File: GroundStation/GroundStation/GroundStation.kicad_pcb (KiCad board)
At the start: 2 copper layers, 42 parts, among them J1 SD_Card_Receptacle, J4 Conn_Coaxial, P1 USB_C_Plug_USB2.0, U1 STM32F103C8Tx, U3 LD1117S33TR_SOT223, U9 NEO-M9N-00B

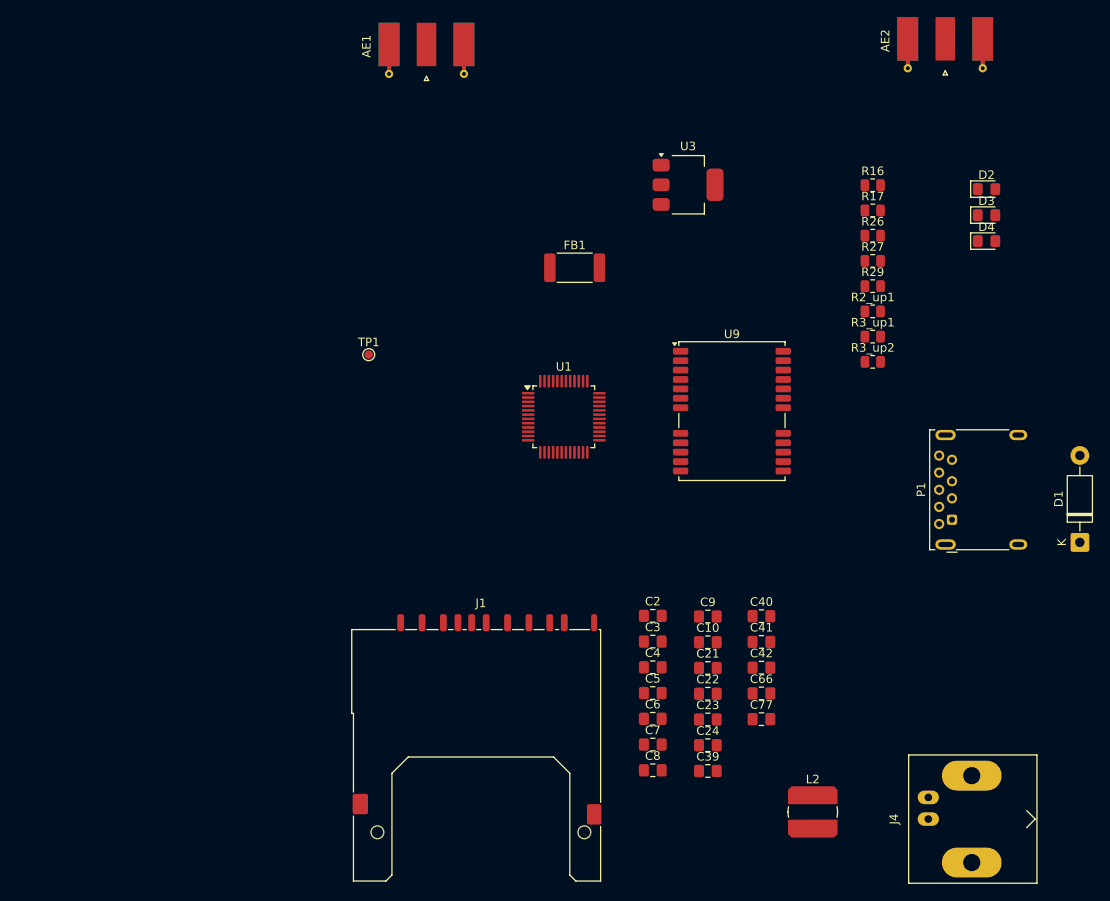
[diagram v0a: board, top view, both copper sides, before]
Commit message: assign package for groundstation
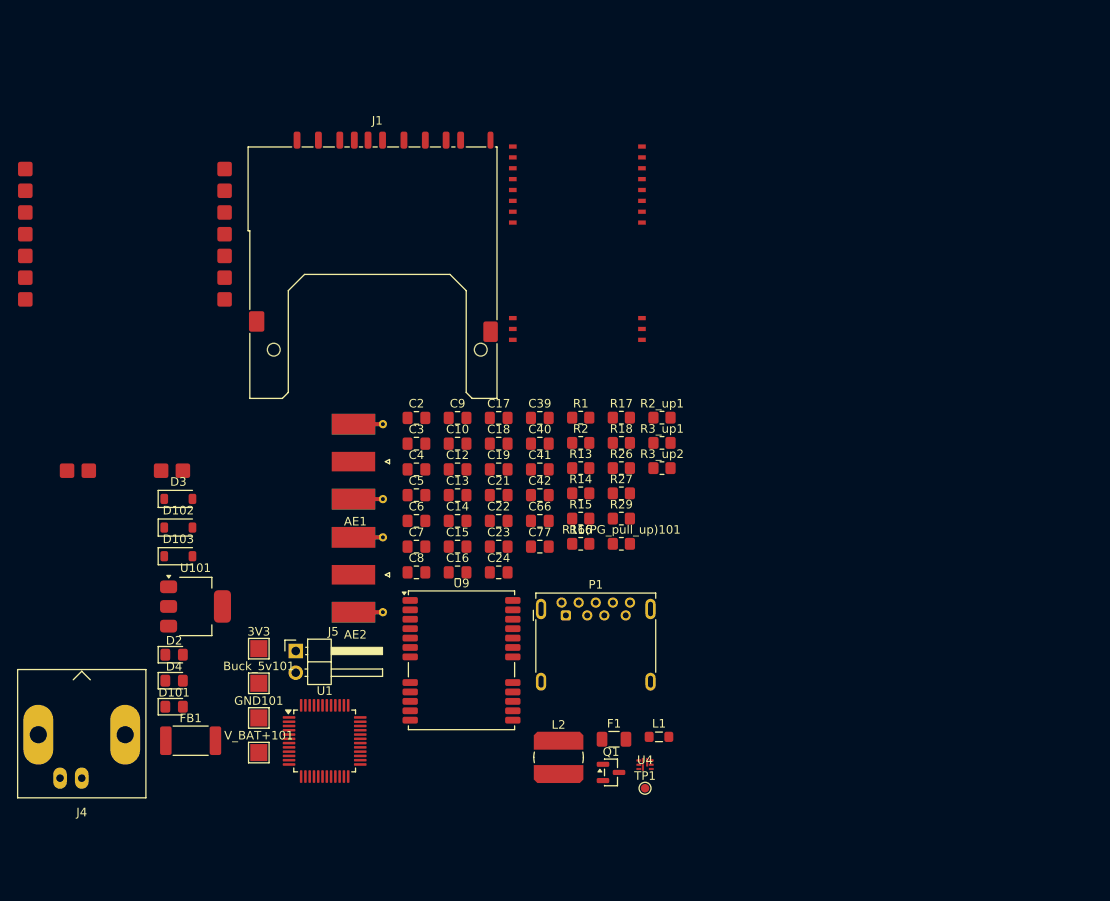
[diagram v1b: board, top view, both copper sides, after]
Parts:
- removed D1: SB120, Diode_THT:D_DO-41_SOD81_P10.16mm_Horizontal
- removed U3: LD1117S33TR_SOT223, Package_TO_SOT_SMD:SOT-223-3_TabPin2
- added 3V3: TestPoint, TestPoint:TestPoint_Pad_2.0x2.0mm, F.Cu at (118.4, 111.2)
- added Buck_5v101: TestPoint, TestPoint:TestPoint_Pad_2.0x2.0mm, F.Cu at (118.4, 115.3)
- added C12: 100n, Capacitor_SMD:C_0805_2012Metric_Pad1.18x1.45mm_HandSolder, F.Cu at (141.7, 90.3)
- added C13: 4.7u, Capacitor_SMD:C_0805_2012Metric_Pad1.18x1.45mm_HandSolder, F.Cu at (141.7, 93.3)
- added C14: 4.7u, Capacitor_SMD:C_0805_2012Metric_Pad1.18x1.45mm_HandSolder, F.Cu at (141.7, 96.3)
- added C15: 4.7u, Capacitor_SMD:C_0805_2012Metric_Pad1.18x1.45mm_HandSolder, F.Cu at (141.7, 99.3)
- added C16: 10p, Capacitor_SMD:C_0805_2012Metric_Pad1.18x1.45mm_HandSolder, F.Cu at (141.7, 102.3)
- added C17: 47u, Capacitor_SMD:C_0805_2012Metric_Pad1.18x1.45mm_HandSolder, F.Cu at (146.5, 84.3)
- added C18: 47u, Capacitor_SMD:C_0805_2012Metric_Pad1.18x1.45mm_HandSolder, F.Cu at (146.5, 87.3)
- added C19: 47u, Capacitor_SMD:C_0805_2012Metric_Pad1.18x1.45mm_HandSolder, F.Cu at (146.5, 90.3)
- added D101: G_5V, LED_SMD:LED_0805_2012Metric_Pad1.15x1.40mm_HandSolder, F.Cu at (108.5, 118.0)
- added D102: TVS, Diode_SMD:D_SOD-123, F.Cu at (109.0, 97.1)
- added D103: TVS, Diode_SMD:D_SOD-123, F.Cu at (109.0, 100.4)
- added E80-900M2213S101: ~, RF:E80-900M2213S, F.Cu at (155.7, 63.5)
- added F1: Fuse, Fuse:Fuse_1206_3216Metric, F.Cu at (159.9, 121.8)
- added GND101: TestPoint, TestPoint:TestPoint_Pad_2.0x2.0mm, F.Cu at (118.4, 119.3)
- added J5: Conn_01x02, Connector_PinHeader_2.54mm:PinHeader_1x02_P2.54mm_Horizontal, F.Cu at (122.7, 111.5)
- added L1: 6.8u, Inductor_SMD:L_0805_2012Metric_Pad1.05x1.20mm_HandSolder, F.Cu at (165.2, 121.5)
- added Q1: TSM3481CX6 RFG, Package_TO_SOT_SMD:SOT-23, F.Cu at (159.6, 125.7)
- added R1: 390k, Resistor_SMD:R_0805_2012Metric_Pad1.20x1.40mm_HandSolder, F.Cu at (156.1, 84.2)
- added R13: 18k, Resistor_SMD:R_0805_2012Metric_Pad1.20x1.40mm_HandSolder, F.Cu at (156.1, 90.1)
- added R14: 220k, Resistor_SMD:R_0805_2012Metric_Pad1.20x1.40mm_HandSolder, F.Cu at (156.1, 93.1)
- added R15: 30k, Resistor_SMD:R_0805_2012Metric_Pad1.20x1.40mm_HandSolder, F.Cu at (156.1, 96.0)
- added R16(PG_pull_up)101: 100k, Resistor_SMD:R_0805_2012Metric_Pad1.20x1.40mm_HandSolder, F.Cu at (160.8, 99.0)
- added R18: 100k, Resistor_SMD:R_0805_2012Metric_Pad1.20x1.40mm_HandSolder, F.Cu at (160.8, 87.2)
- added R2: 100k, Resistor_SMD:R_0805_2012Metric_Pad1.20x1.40mm_HandSolder, F.Cu at (156.1, 87.2)
- added U101: LD1117S33TR_SOT223, Package_TO_SOT_SMD:SOT-223-3_TabPin2, F.Cu at (111.0, 106.3)
- added U2: E22-400T30S_LoRa, Library:e22-400t30s_Package, F.Cu at (90.3, 50.8)
- added U4: TPS54538RQFR, RF:TPS54538RQFR, F.Cu at (163.6, 124.8)
- added V_BAT+101: TestPoint, TestPoint:TestPoint_Pad_2.0x2.0mm, F.Cu at (118.4, 123.4)
- D2: value G_5V -> B_3V3
- D3: value B_3V3 -> TVS; footprint LED_SMD:LED_0805_2012Metric_Pad1.15x1.40mm_HandSolder -> Diode_SMD:D_SOD-123
- R16, R17, R26, R27, R29, R2_up1, R3_up1, R3_up2: footprint Resistor_SMD:R_0805_2012Metric -> Resistor_SMD:R_0805_2012Metric_Pad1.20x1.40mm_HandSolder
- moved D2 109.5 mm to (108.5, 111.9)
- moved D4 108.0 mm to (108.5, 115.0)
- moved D3 100.2 mm to (109.0, 93.7)
- moved J4 99.1 mm to (97.7, 126.4), turned to 0 degrees
- moved AE2 90.9 mm to (131.2, 102.6), turned to 0 degrees
- moved FB1 71.2 mm to (110.4, 122.0)
- moved TP1 60.1 mm to (163.6, 127.6)
- moved J1 57.7 mm to (132.3, 64.3)
- moved R16 54.1 mm to (156.1, 99.0)
- moved AE1 47.5 mm to (131.2, 89.4), turned to 0 degrees
- moved U1 47.1 mm to (126.1, 122.0)
- moved P1 46.5 mm to (154.3, 107.3), turned to 0 degrees
- moved C39 45.7 mm to (151.3, 84.3)
- moved U9 43.0 mm to (142.1, 112.6)
- moved R26 40.0 mm to (160.8, 90.1)
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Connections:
- C21 pad 1: 3.3V -> +3.3V
- C22 pad 1: 3.3V -> +3.3V
- C23 pad 1: +5V -> Net-(D102-A1)
- C24 pad 1: 3.3V -> +3.3V
- D3 pad 2: Net-(D3-A) -> Net-(D3-A2)
- R16 pad 1: Net-(D2-A) -> Net-(D101-A)
- R16 pad 2: +5V -> BUCK_5V
- R17 pad 1: Net-(D3-A) -> Net-(D2-A)
- R17 pad 2: 3.3V -> +3.3V
